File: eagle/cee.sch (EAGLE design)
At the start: 56 parts, among them IC1 IC1, J1 SOLDERJUMPERNC2

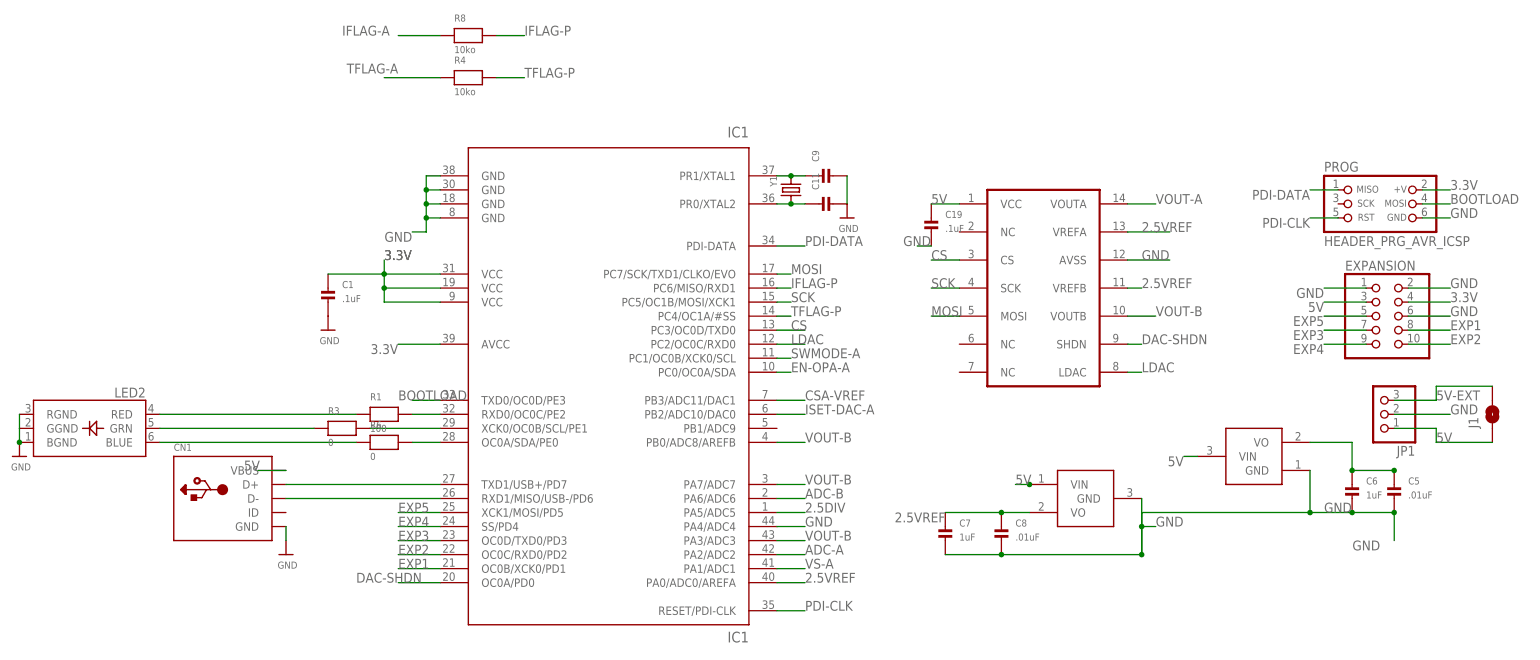
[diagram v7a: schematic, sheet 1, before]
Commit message: Connect CSA EN pin
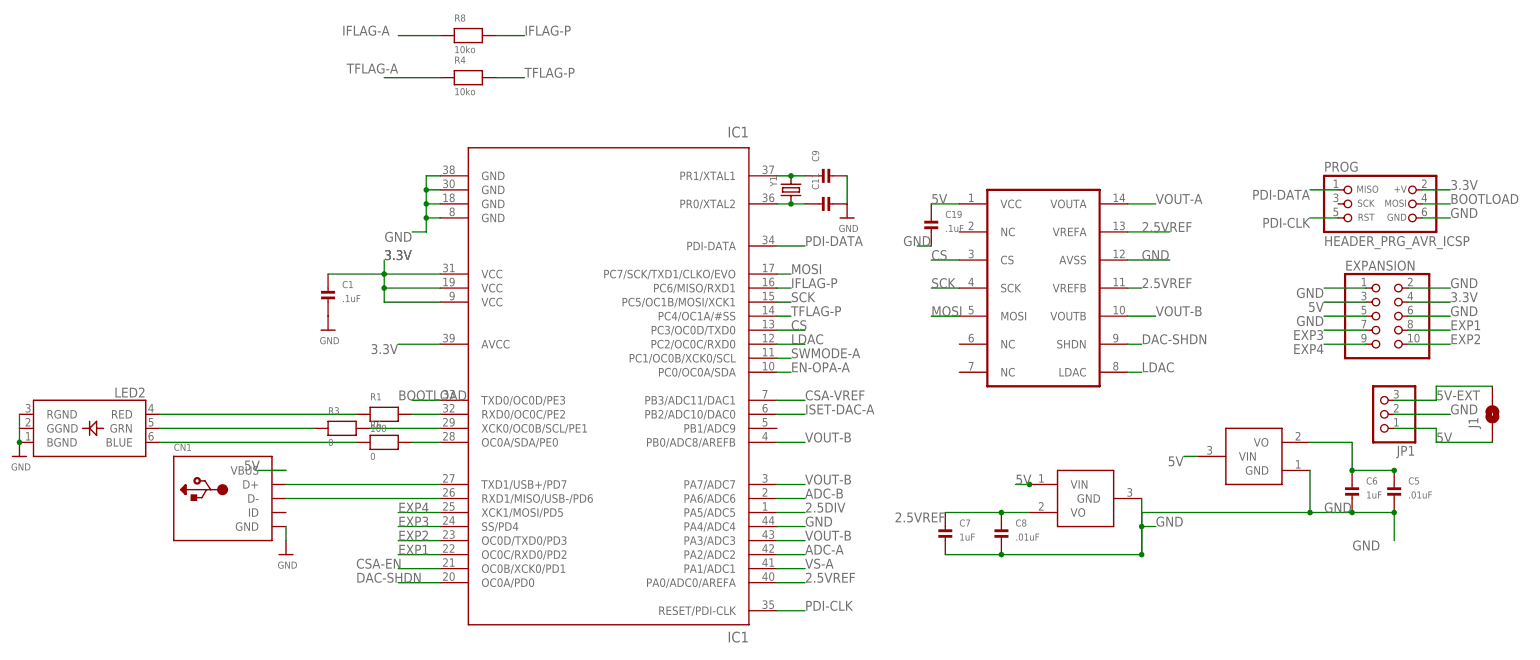
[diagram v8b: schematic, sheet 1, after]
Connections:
- removed net EN-CSA: U$13.EN/CAL
- removed net EXP5: EXPANSION.5, IC1.XCK1/MOSI/PD5
- new net CSA-EN: IC1.OC0B/XCK0/PD1, U$13.EN/CAL
- net EXP1: now also IC1.OC0C/RXD0/PD2; no longer IC1.OC0B/XCK0/PD1
- net EXP2: now also IC1.OC0D/TXD0/PD3; no longer IC1.OC0C/RXD0/PD2
- net EXP3: now also IC1.SS/PD4; no longer IC1.OC0D/TXD0/PD3
- net EXP4: now also IC1.XCK1/MOSI/PD5; no longer IC1.SS/PD4
- net GND: now also EXPANSION.5
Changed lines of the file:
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@@
 <label x="218.44" y="53.34" size="1.778" layer="95"/>
+</segment>
+<segment>
+<pinref part="EXPANSION" gate="A" pin="5"/>
+<wire x1="203.2" y1="53.34" x2="195.58" y2="53.34" width="0.254" layer="91"/>
+<label x="195.58" y="53.34" size="1.778" layer="95" rot="R180"/>
 </segment>
 </net>
@@
 <net name="EXP3" class="0">
 <segment>
-<pinref part="IC1" gate="G$1" pin="OC0D/TXD0/PD3"/>
-<wire x1="35.56" y1="12.7" x2="27.94" y2="12.7" width="0.254" layer="91"/>
-<label x="27.94" y="12.7" size="1.778" layer="95"/>
-</segment>
-<segment>
 <pinref part="EXPANSION" gate="A" pin="7"/>
 <wire x1="203.2" y1="50.8" x2="195.58" y2="50.8" width="0.254" layer="91"/>
 <label x="195.58" y="50.8" size="1.778" layer="95" rot="R180"/>
 </segment>
-</net>
-<net name="EXP2" class="0">
+<segment>
+<pinref part="IC1" gate="G$1" pin="SS/PD4"/>
+<wire x1="35.56" y1="15.24" x2="27.94" y2="15.24" width="0.254" layer="91"/>
+<label x="27.94" y="15.24" size="1.778" layer="95"/>
+</segment>
+</net>
+<net name="EXP1" class="0">
+<segment>
+<pinref part="EXPANSION" gate="A" pin="8"/>
+<wire x1="210.82" y1="50.8" x2="218.44" y2="50.8" width="0.254" layer="91"/>
+<label x="218.44" y="50.8" size="1.778" layer="95"/>
+</segment>
 <segment>
 <pinref part="IC1" gate="G$1" pin="OC0C/RXD0/PD2"/>
 <wire x1="35.56" y1="10.16" x2="27.94" y2="10.16" width="0.254" layer="91"/>
 <label x="27.94" y="10.16" size="1.778" layer="95"/>
-</segment>
-<segment>
-<pinref part="EXPANSION" gate="A" pin="10"/>
-<wire x1="210.82" y1="48.26" x2="218.44" y2="48.26" width="0.254" layer="91"/>
-<label x="218.44" y="48.26" size="1.778" layer="95"/>
-</segment>
-</net>
-<net name="EXP1" class="0">
-<segment>
-<pinref part="IC1" gate="G$1" pin="OC0B/XCK0/PD1"/>
-<wire x1="35.56" y1="7.62" x2="27.94" y2="7.62" width="0.254" layer="91"/>
-<label x="27.94" y="7.62" size="1.778" layer="95"/>
-</segment>
-<segment>
-<pinref part="EXPANSION" gate="A" pin="8"/>
-<wire x1="210.82" y1="50.8" x2="218.44" y2="50.8" width="0.254" layer="91"/>
-<label x="218.44" y="50.8" size="1.778" layer="95"/>
 </segment>
 </net>
@@
 <net name="EXP4" class="0">
 <segment>
-<pinref part="IC1" gate="G$1" pin="SS/PD4"/>
-<wire x1="35.56" y1="15.24" x2="27.94" y2="15.24" width="0.254" layer="91"/>
-<label x="27.94" y="15.24" size="1.778" layer="95"/>
-</segment>
-<segment>
 <pinref part="EXPANSION" gate="A" pin="9"/>
 <wire x1="203.2" y1="48.26" x2="195.58" y2="48.26" width="0.254" layer="91"/>
 <label x="195.58" y="48.26" size="1.778" layer="95" rot="R180"/>
 </segment>
+<segment>
+<pinref part="IC1" gate="G$1" pin="XCK1/MOSI/PD5"/>
+<wire x1="35.56" y1="17.78" x2="27.94" y2="17.78" width="0.254" layer="91"/>
+<label x="27.94" y="17.78" size="1.778" layer="95"/>
+</segment>
 </net>
 <net name="CSA-VREF" class="0">
@@
 </segment>
 </net>
-<net name="EXP5" class="0">
-<segment>
-<pinref part="IC1" gate="G$1" pin="XCK1/MOSI/PD5"/>
-<wire x1="35.56" y1="17.78" x2="27.94" y2="17.78" width="0.254" layer="91"/>
-<label x="27.94" y="17.78" size="1.778" layer="95"/>
-</segment>
-<segment>
-<pinref part="EXPANSION" gate="A" pin="5"/>
-<wire x1="203.2" y1="53.34" x2="195.58" y2="53.34" width="0.254" layer="91"/>
-<label x="195.58" y="53.34" size="1.778" layer="95" rot="R180"/>
-</segment>
-</net>
 <net name="2.5DIV" class="0">
 <segment>
@@
 <wire x1="96.52" y1="17.78" x2="101.6" y2="17.78" width="0.254" layer="91"/>
 <label x="101.6" y="17.78" size="1.778" layer="95"/>
+</segment>
+</net>
+<net name="CSA-EN" class="0">
+<segment>
+<pinref part="IC1" gate="G$1" pin="OC0B/XCK0/PD1"/>
+<wire x1="35.56" y1="7.62" x2="27.94" y2="7.62" width="0.254" layer="91"/>
+<label x="20.32" y="7.62" size="1.778" layer="95"/>
+</segment>
+</net>
+<net name="EXP2" class="0">
+<segment>
+<pinref part="IC1" gate="G$1" pin="OC0D/TXD0/PD3"/>
+<wire x1="35.56" y1="12.7" x2="27.94" y2="12.7" width="0.254" layer="91"/>
+<label x="27.94" y="12.7" size="1.778" layer="95"/>
+</segment>
+<segment>
+<pinref part="EXPANSION" gate="A" pin="10"/>
+<wire x1="210.82" y1="48.26" x2="218.44" y2="48.26" width="0.254" layer="91"/>
+<label x="218.44" y="48.26" size="1.778" layer="95"/>
 </segment>
 </net>
@@
 </segment>
 </net>
-<net name="EN-CSA" class="0">
+<net name="CSA-EN" class="0">
 <segment>
 <pinref part="U$13" gate="G$1" pin="EN/CAL"/>
